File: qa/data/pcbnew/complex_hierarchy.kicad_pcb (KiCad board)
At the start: 2 copper layers, 100.3 x 80 mm, 72 parts, among them P1 CONN_2, P2 CONN_2, P3 CONN_2, P4 CONN_2, P5 CONN_2, P6 CONN_2, Q1 MPAS92, Q2 MPAS42, Q3 MPAS92, Q4 MPAS42, Q5 MPAS92, Q6 MPAS42, Q7 MPAS92, Q8 MPAS42, U1 ICL7660, U2 78L05, U3 LM358N, U4 LM358N

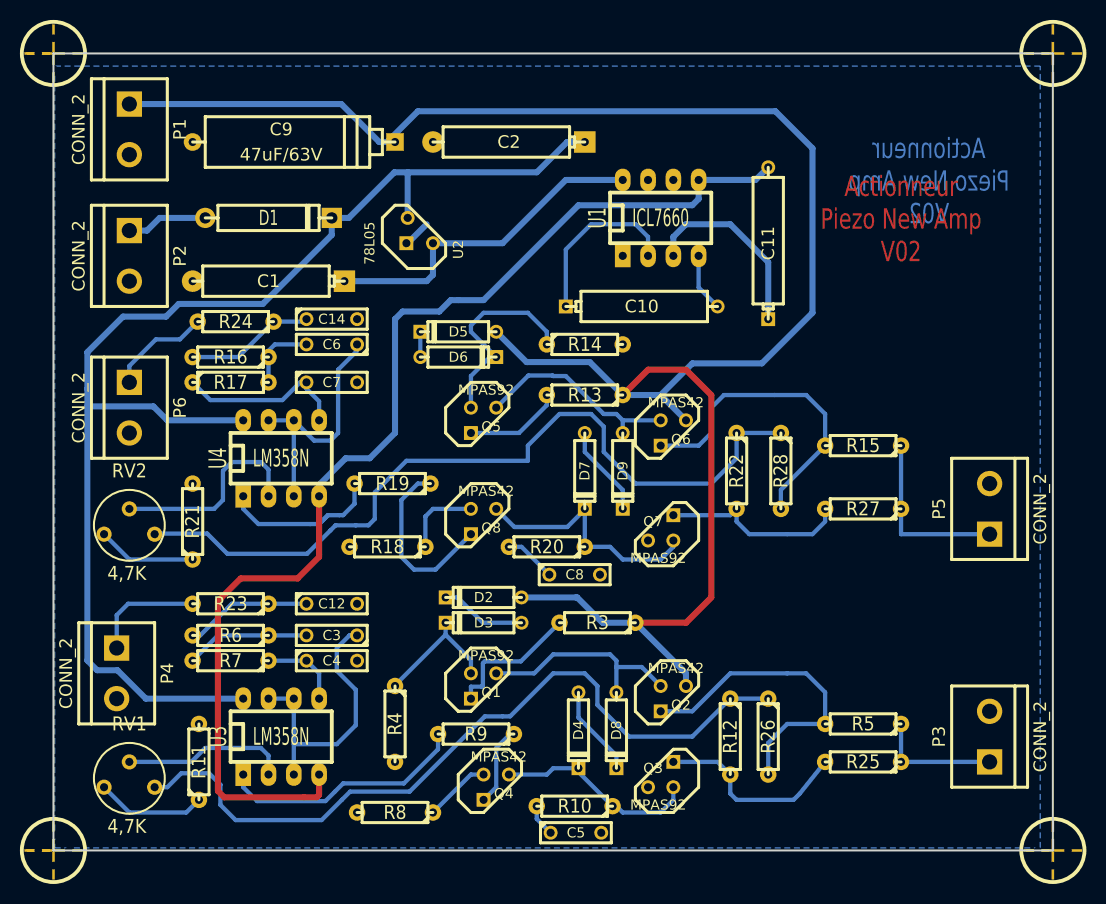
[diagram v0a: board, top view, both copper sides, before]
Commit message: Update qa tests to use new zone fill algo
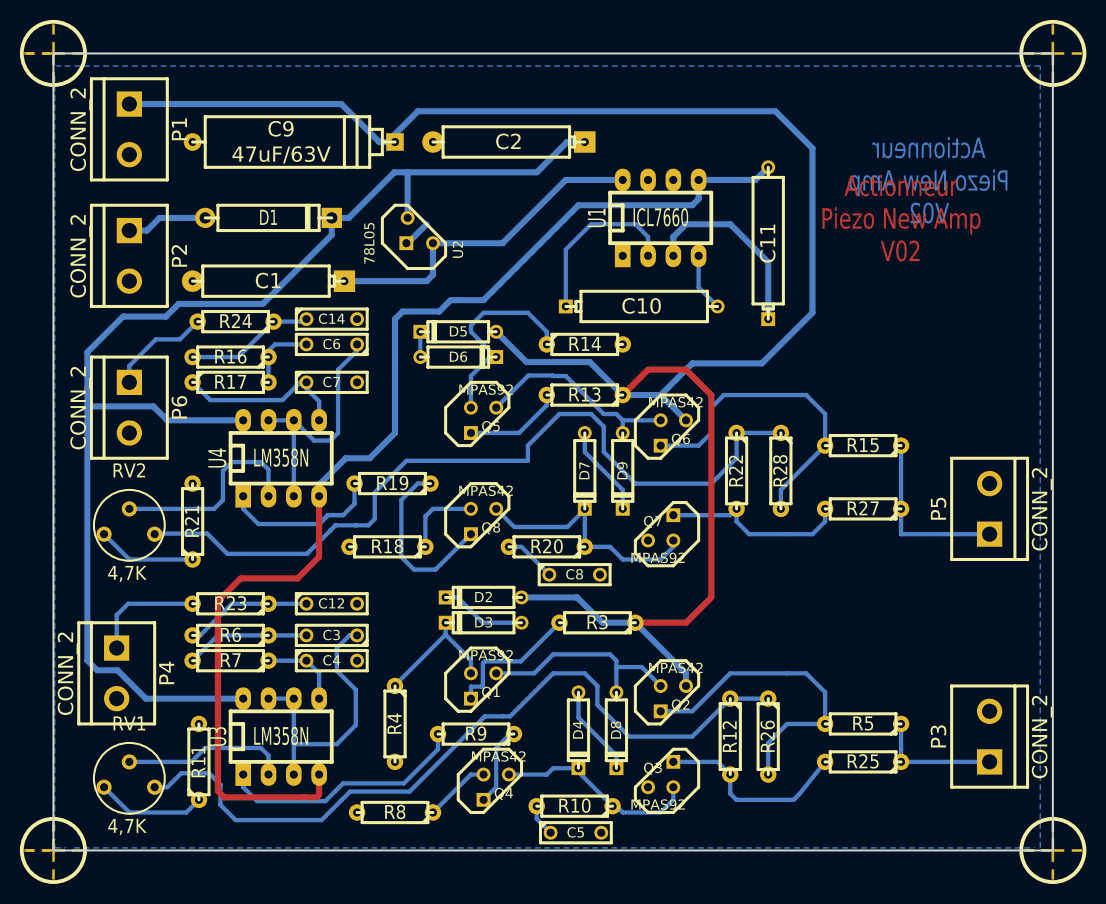
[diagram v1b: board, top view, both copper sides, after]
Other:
- net class Default removed
- net class power removed
